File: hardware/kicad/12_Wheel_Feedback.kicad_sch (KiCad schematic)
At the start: 22 parts, among them U23 ADS7038IRTER, U27 MA735GGU-P, U28 TPS22919DCKR

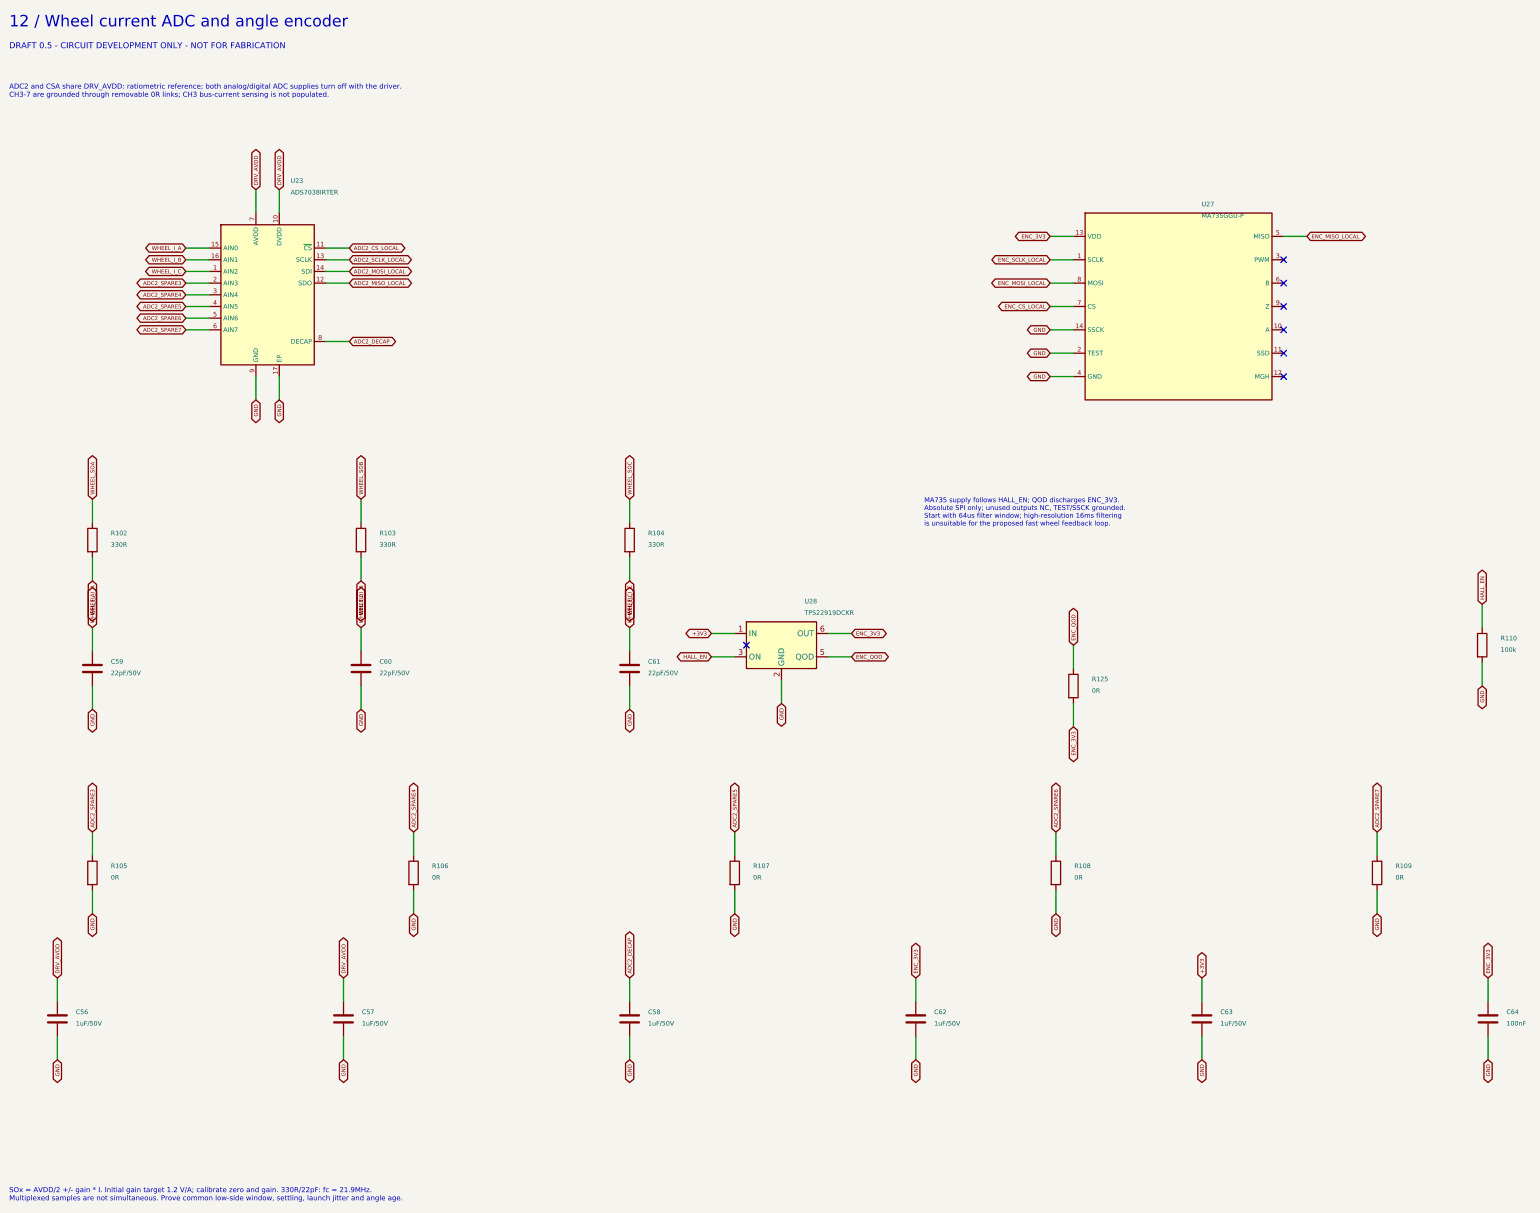
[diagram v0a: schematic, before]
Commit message: Place motherboard, add upright encoder PCB and route logic buck
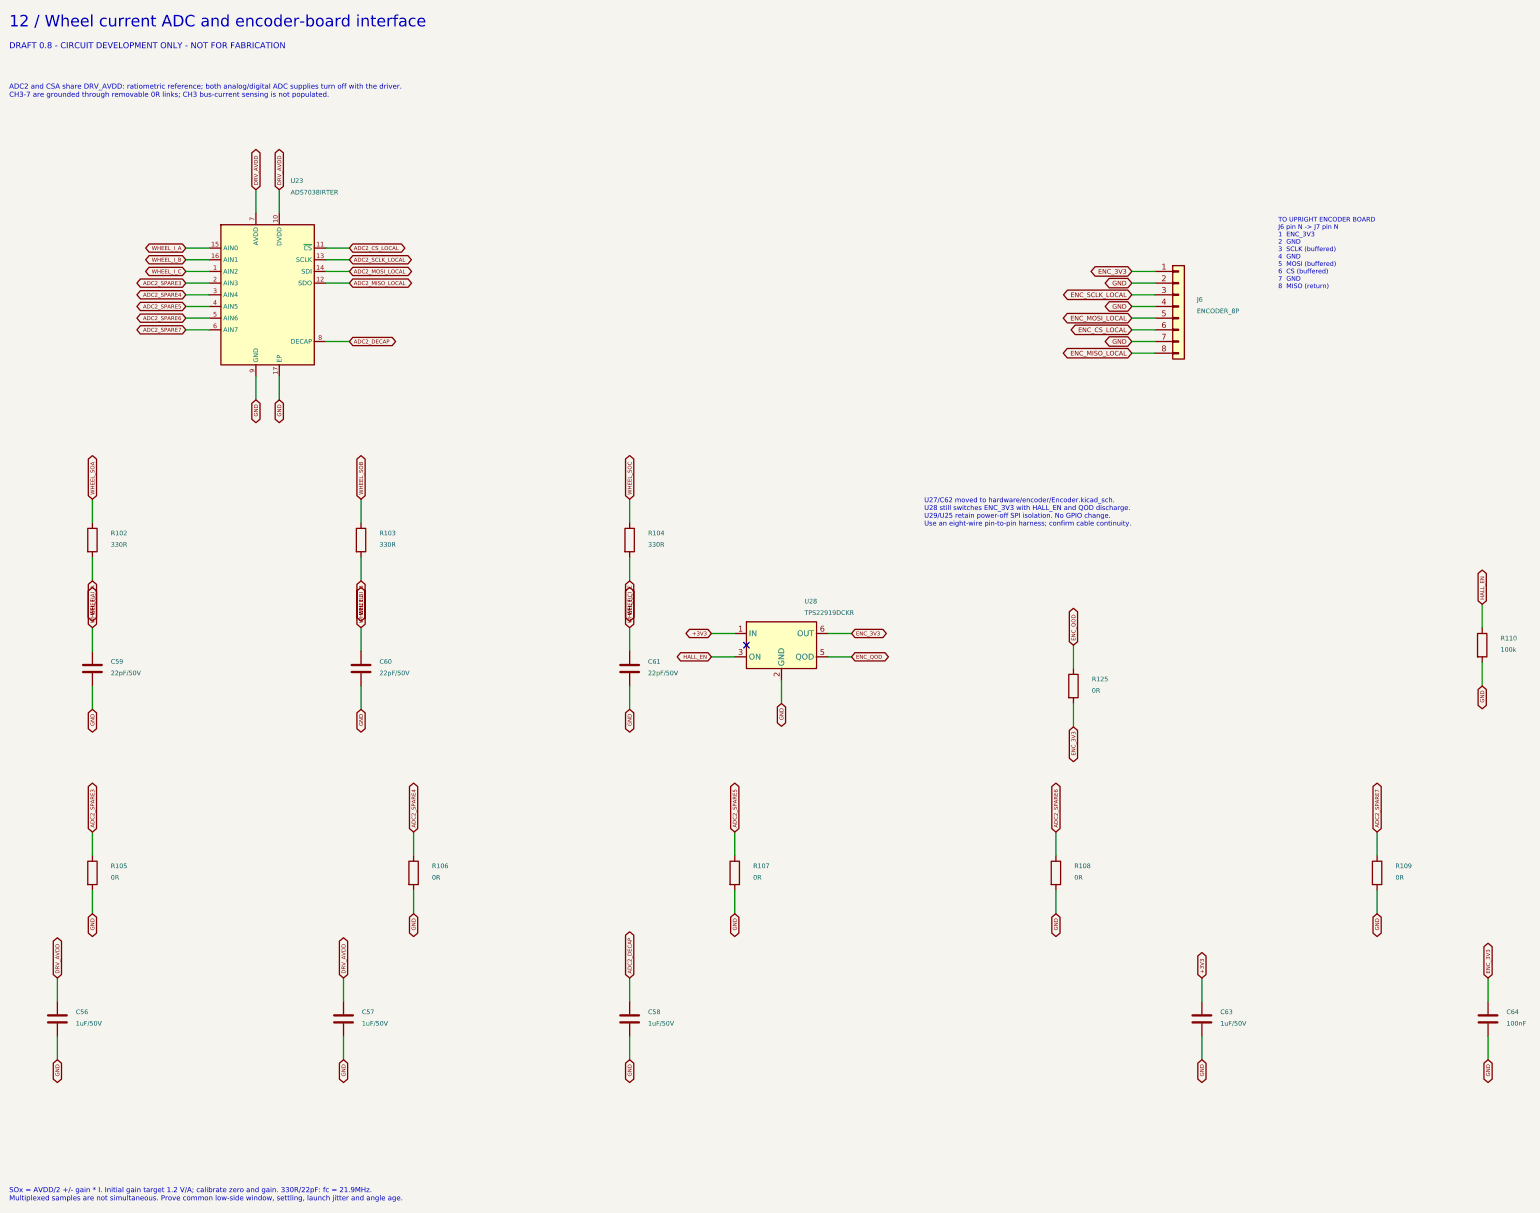
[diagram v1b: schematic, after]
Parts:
- removed C62: 1uF/50V, Capacitor_SMD:C_0603_1608Metric, symbol Device:C
- removed U27: MA735GGU-P, MagMouse:MPS_UTQFN14_2x2, symbol MagMouse:MA735GGU
- added J6: ENCODER_8P, Connector_JST:JST_SH_SM08B-SRSS-TB_1x08-1MP_P1.00mm_Horizontal, symbol Connector_Generic:Conn_01x08
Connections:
- net ENC_3V3: now also J6.1 (Pin_1)
- net ENC_CS_LOCAL: now also J6.6 (Pin_6)
- net ENC_MISO_LOCAL: now also J6.8 (Pin_8)
- net ENC_MOSI_LOCAL: now also J6.5 (Pin_5)
- net ENC_SCLK_LOCAL: now also J6.3 (Pin_3)
- net GND: now also J6.2 (Pin_2), J6.4 (Pin_4), J6.7 (Pin_7)
- no-connect marks 7 -> 1
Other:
- note added: "12 / Wheel current ADC and encoder-board interface"
- note added: "DRAFT 0.8 - CIRCUIT DEVELOPMENT ONLY - NOT FOR FABRICATION"
- note added: "TO UPRIGHT ENCODER BOARD J6 pin N -> J7 pin N 1 ENC_3V3 2 GND 3 SCLK (buffered) 4 GND 5 MOSI (buffered) 6 CS (buffered) 7 GND 8 MISO (return)"
- note added: "U27/C62 moved to hardware/encoder/Encoder.kicad_sch. U28 still switches ENC_3V3 with HALL_EN and QOD discharge. U29/U25 retain power-off SPI isolation. No GPIO change. Use an eight-wire pin-to-pin harness; confirm cable continuity."
- note removed: "12 / Wheel current ADC and angle encoder"
- note removed: "DRAFT 0.5 - CIRCUIT DEVELOPMENT ONLY - NOT FOR FABRICATION"
- note removed: "MA735 supply follows HALL_EN; QOD discharges ENC_3V3. Absolute SPI only; unused outputs NC, TEST/SSCK grounded. Start with 64us filter window; high-resolution 16ms filtering is unsuitable for the proposed fast wheel feedback loop."
